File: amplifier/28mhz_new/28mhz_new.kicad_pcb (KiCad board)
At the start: 2 copper layers, 73.2 x 56 mm, 36 parts, among them J1 Conn_Coaxial_Small, J1 GPIO, M1 RD16HHF1

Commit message: moved a few things further apart
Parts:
- moved C1 2.02 mm to (114.8, 100.0)
- moved C2 1.00 mm to (110.8, 97.0)
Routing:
- net Net-(M1-D): track 38.9 -> 41.9 mm
- net Net-(C2-Pad1): track 7.73 -> 6.73 mm
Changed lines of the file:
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@@
 	(footprint "Capacitor_SMD:C_0805_2012Metric_Pad1.18x1.45mm_HandSolder"
 		(layer "F.Cu")
-		(at 115 98.0375 -90)
+		(at 114.75 100.0375 -90)
 		(descr "Capacitor SMD 0805 (2012 Metric), square (rectangular) end terminal, IPC_7351 nominal with elongated pad for handsoldering. (Body size source: IPC-SM-782 page 76, https://www.pcb-3d.com/wordpress/wp-content/uploads/ipc-sm-782a_amendment_1_and_2.pdf, https://docs.google.com/spreadsheets/d/1BsfQQcO9C6DZCsRaXUlFlo91Tg2WpOkGARC1WS5S8t0/edit?usp=sharing), generated with kicad-footprint-generator")
 		(tags "capacitor handsolder")
@@
 	(footprint "Capacitor_SMD:C_0805_2012Metric_Pad1.18x1.45mm_HandSolder"
 		(layer "F.Cu")
-		(at 111.75 97)
+		(at 110.75 97)
 		(descr "Capacitor SMD 0805 (2012 Metric), square (rectangular) end terminal, IPC_7351 nominal with elongated pad for handsoldering. (Body size source: IPC-SM-782 page 76, https://www.pcb-3d.com/wordpress/wp-content/uploads/ipc-sm-782a_amendment_1_and_2.pdf, https://docs.google.com/spreadsheets/d/1BsfQQcO9C6DZCsRaXUlFlo91Tg2WpOkGARC1WS5S8t0/edit?usp=sharing), generated with kicad-footprint-generator")
 		(tags "capacitor handsolder")
@@
 	)
 	(segment
-		(start 115 97)
-		(end 118.305 97)
+		(start 111.7875 97.5875)
+		(end 111.7875 97)
 		(width 1)
 		(layer "F.Cu")
@@
 	)
 	(segment
-		(start 115 97)
-		(end 112.7875 97)
+		(start 113.2 99)
+		(end 111.7875 97.5875)
 		(width 1)
 		(layer "F.Cu")
@@
 	)
 	(segment
-		(start 109.4625 95.75)
-		(end 110.7125 97)
+		(start 116.345 99)
+		(end 114.75 99)
 		(width 1)
 		(layer "F.Cu")
-		(net 3)
+		(net 2)
+	)
+	(segment
+		(start 118.305 97.04)
+		(end 116.345 99)
+		(width 1)
+		(layer "F.Cu")
+		(net 2)
+	)
+	(segment
+		(start 114.75 99)
+		(end 113.2 99)
+		(width 1)
+		(layer "F.Cu")
+		(net 2)
 	)
 	(segment
 		(start 103.5 95.75)
-		(end 109.4625 95.75)
+		(end 108.4625 95.75)
+		(width 1)
+		(layer "F.Cu")
+		(net 3)
+	)
+	(segment
+		(start 108.4625 95.75)
+		(end 109.7125 97)
 		(width 1)
 		(layer "F.Cu")

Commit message: SEND IT (in the morning once i have sanity checked)
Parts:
- added J2: 694106301002, barreljack:694106301002_1, F.Cu at (69.2, 62.6)
- B1: renamed from J1; value Conn_Coaxial_Small -> CONBNC002
- moved R1 11.0 mm to (80.8, 73.5), turned to 90 degrees
- moved RB2 3.13 mm to (82.0, 80.0), turned to 180 degrees
- moved CB1 2.00 mm to (82.0, 77.8)
- moved QN1 2.00 mm to (86.0, 82.9)
- moved QN2 2.00 mm to (86.0, 76.6)
- moved RB3 2.00 mm to (83.0, 74.7)
- moved RE1 2.00 mm to (87.0, 87.9)
- moved RB1 1.61 mm to (83.0, 85.2), turned to -90 degrees
- moved RC1 1.52 mm to (90.0, 75.0), turned to -90 degrees
- moved L1 0.10 mm to (101.7, 70.2)
- moved H1 0.08 mm to (122.5, 81.8)
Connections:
- net /RF_IN renamed /GPIO4/GPCLK0
- B1 pad MH1: (no net) -> unconnected-(B1-PadMH1)
- B1 pad MH2: (no net) -> unconnected-(B1-PadMH2)
- J1 pad 1: (no net) -> +3V3
- J1 pad 10: (no net) -> /GPIO15/RXD0
- J1 pad 11: (no net) -> /GPIO17
- J1 pad 12: (no net) -> /GPIO18/PCM.CLK
- J1 pad 13: (no net) -> /GPIO27
- J1 pad 14: (no net) -> 0
- J1 pad 15: (no net) -> /GPIO22
- J1 pad 16: (no net) -> /GPIO23
- J1 pad 17: (no net) -> +3V3
- J1 pad 18: (no net) -> /GPIO24
- J1 pad 19: (no net) -> /GPIO10/SPI0.MOSI
- J1 pad 2: (no net) -> +5V
- J1 pad 20: (no net) -> 0
- J1 pad 21: (no net) -> /GPIO9/SPI0.MISO
- J1 pad 22: (no net) -> /GPIO25
- J1 pad 23: (no net) -> /GPIO11/SPI0.SCLK
- J1 pad 24: (no net) -> /GPIO8/SPI0.CE0
- J1 pad 25: (no net) -> 0
- J1 pad 26: (no net) -> /GPIO7/SPI0.CE1
- J1 pad 27: (no net) -> /ID_SDA
- J1 pad 28: (no net) -> /ID_SCL
- J1 pad 29: (no net) -> /GPIO5
- J1 pad 3: (no net) -> /GPIO2/SDA1
- J1 pad 30: (no net) -> 0
- J1 pad 31: (no net) -> /GPIO6
- J1 pad 32: (no net) -> /GPIO12/PWM0
- J1 pad 33: (no net) -> /GPIO13/PWM1
- J1 pad 34: (no net) -> 0
- J1 pad 35: (no net) -> /GPIO19/PCM.FS
- J1 pad 36: (no net) -> /GPIO16
- J1 pad 37: (no net) -> /GPIO26
- J1 pad 38: (no net) -> /GPIO20/PCM.DIN
- J1 pad 39: (no net) -> 0
- J1 pad 4: (no net) -> +5V
- J1 pad 40: (no net) -> /GPIO21/PCM.DOUT
- J1 pad 5: (no net) -> /GPIO3/SCL1
- J1 pad 6: (no net) -> 0
- J1 pad 8: (no net) -> /GPIO14/TXD0
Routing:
- net Net-(QN1-B): track 5.25 -> 17.2 mm
- net /GPIO4/GPCLK0: track 21.0 -> 9.44 mm
- net /VCC: track 29.3 -> 39.8 mm
- net Net-(QN2-C): track 8.64 -> 7.62 mm
- net 0: vias 36 -> 56
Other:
- board text removed: "HEATSINK FOR RD16HHF1 OTHER PUSH PULL POWER CONNECTORS BNC CONNECTORS RPI HAT"

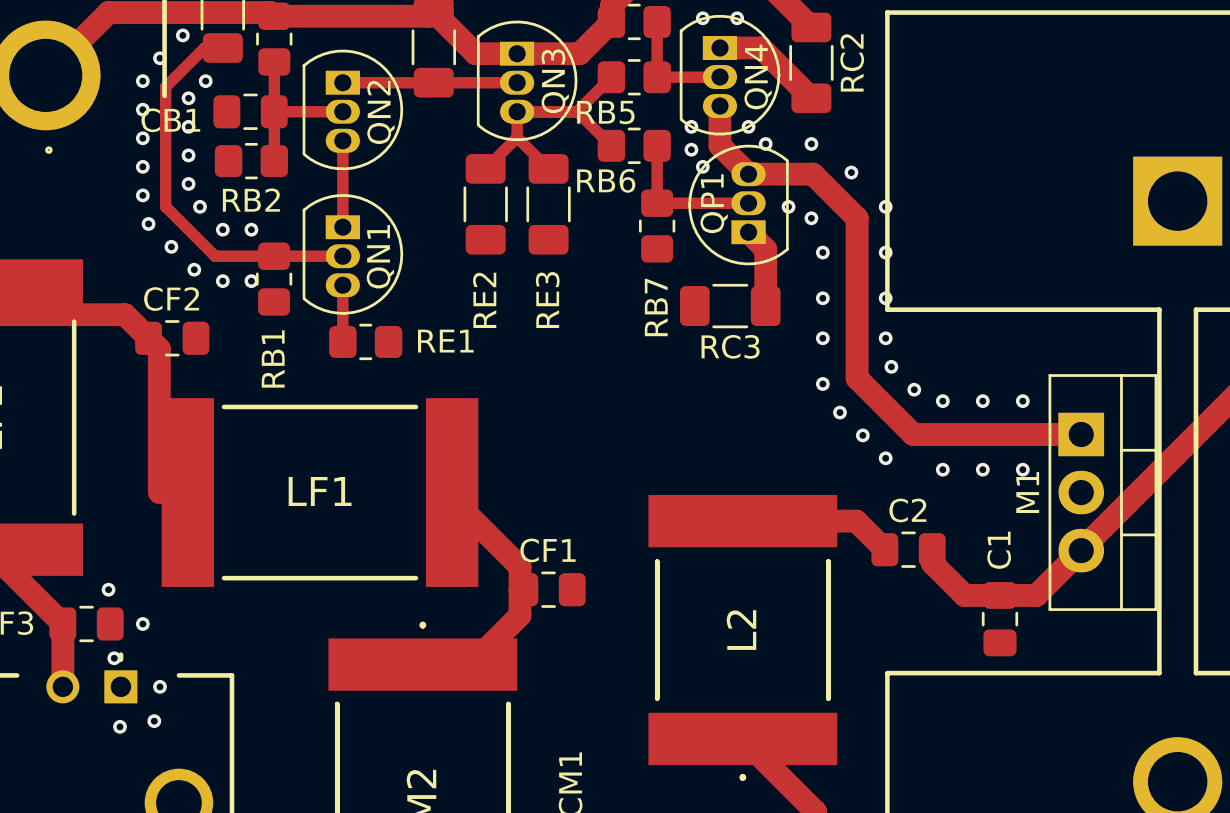
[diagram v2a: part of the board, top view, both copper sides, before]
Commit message: Add zero ohm resistors
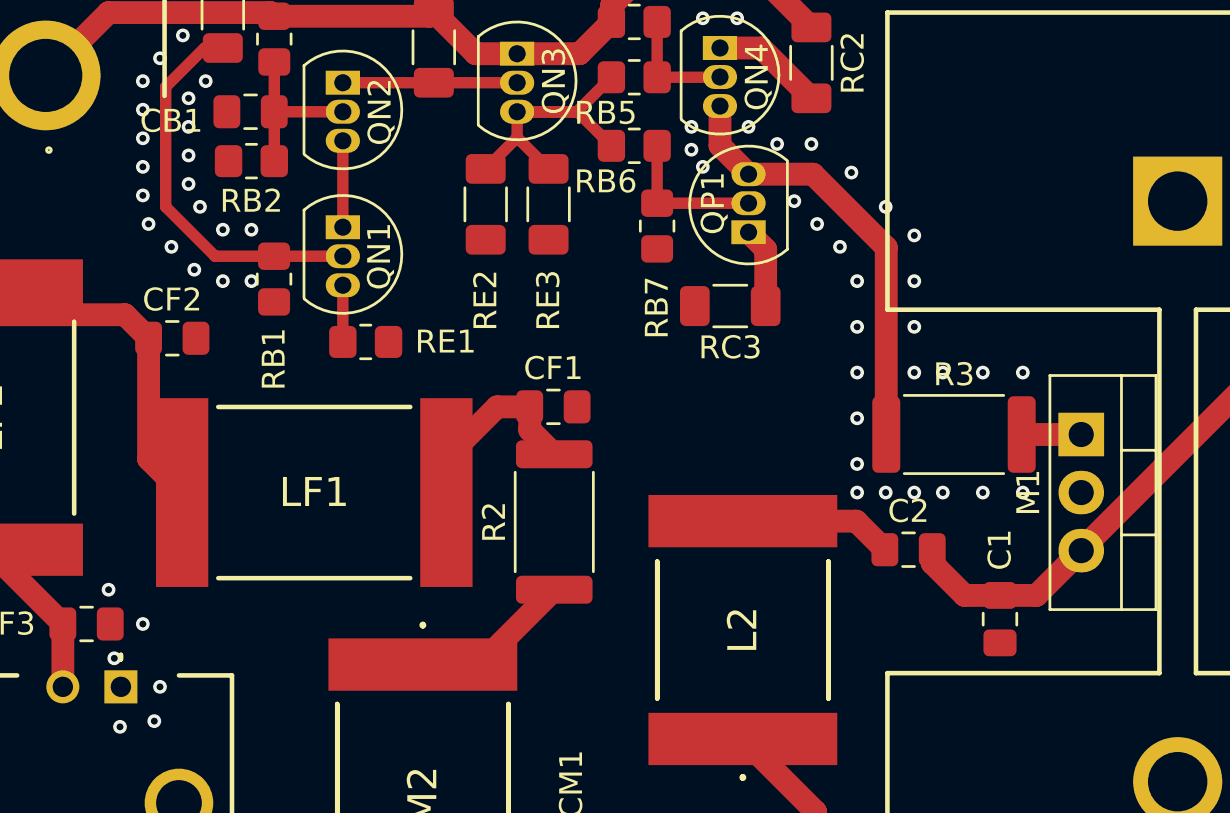
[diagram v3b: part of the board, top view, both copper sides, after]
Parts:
- added R2: 0, Resistor_SMD:R_2512_6332Metric, F.Cu at (95.2, 95.8)
- added R3: 0, Resistor_SMD:R_2512_6332Metric, F.Cu at (112.7, 92.0)
- moved CF1 8.00 mm to (95.2, 90.8)
- moved LF1 0.25 mm to (84.8, 94.5)
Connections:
- LM2 pad 1: Net-(CF1-Pad1) -> Net-(LM2-Pad1)
- QN4 pad 3: Net-(M1-G) -> Net-(QN4-E)
- QP1 pad 3: Net-(M1-G) -> Net-(QN4-E)
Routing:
- net Net-(M1-G): track 26.9 -> 2.61 mm
- net Net-(QN4-E): track 0.00 -> 19.0 mm
- net Net-(LM2-Pad1): track 0.00 -> 7.11 mm
- net Net-(CF1-Pad1): track 11.9 -> 10.1 mm
- net 0: vias 56 -> 57
